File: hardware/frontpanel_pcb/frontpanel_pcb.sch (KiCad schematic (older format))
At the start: 15 parts, among them J1 Conn_02x06_Top_Bottom, Q1 BSS138, U1 291V1, U2 NHD-2.8-25664

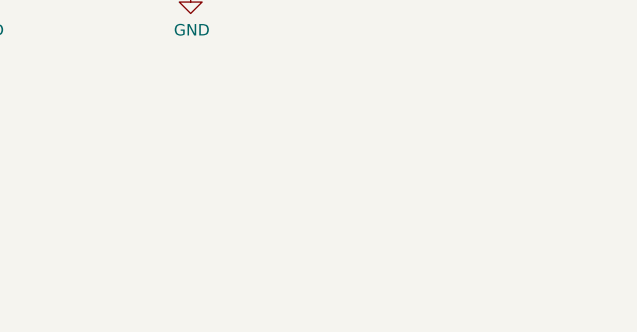
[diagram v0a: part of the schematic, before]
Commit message: hardware: add 2U front / back panel, add Si570 board
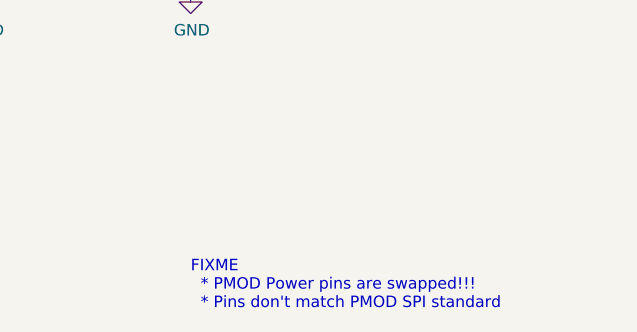
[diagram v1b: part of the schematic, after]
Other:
- note added: "FIXME\n * PMOD Power pins are swapped!!!\n * Pins don't match PMOD SPI standard"
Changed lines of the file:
@@
 Text Label 3600 2250 0    50   ~ 0
 JA8
+Text Notes 7600 6850 0    50   ~ 0
+FIXME\n  * PMOD Power pins are swapped!!!\n  * Pins don't match PMOD SPI standard
 $EndSCHEMATC

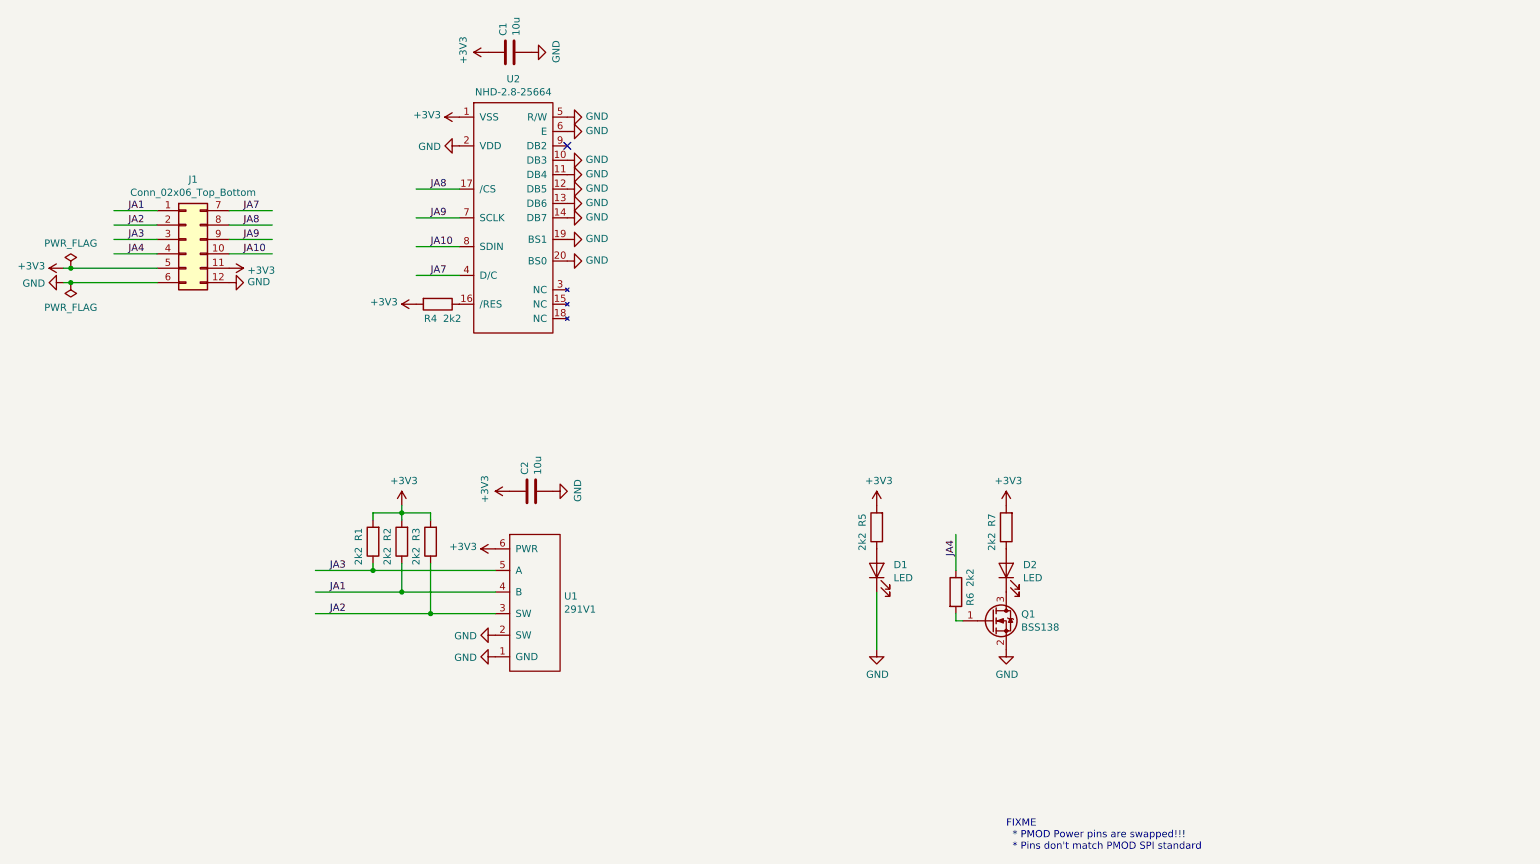
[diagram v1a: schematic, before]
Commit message: Fix display board PMOD pinout
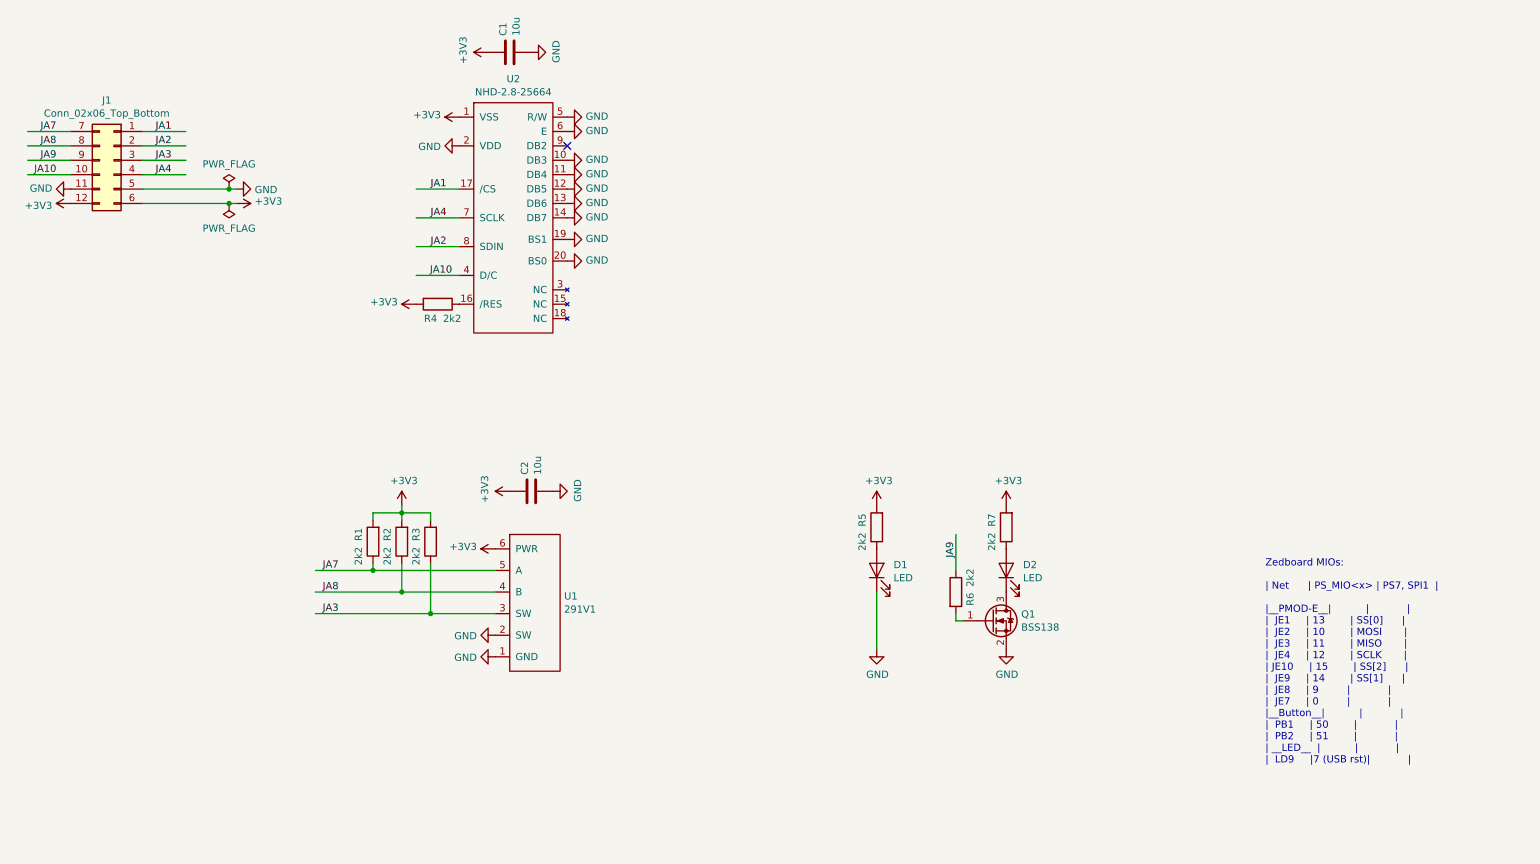
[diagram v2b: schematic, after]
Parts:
- J1: footprint Connector_PinHeader_2.54mm:PinHeader_2x06_P2.54mm_Horizontal -> pmod-conn_6x2:pmod_pin_array_6x2
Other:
- note added: "Zedboard MIOs:\n\n| Net | PS_MIO<x> | PS7, SPI1 |\n\n|__PMOD-E__| | |\n| JE1 | 13 | SS[0] |\n| JE2 | 10 | MOSI |\n| JE3 | 11 | MISO |\n| JE4 | 12 | SCLK |\n| JE10 | 15 | SS[2] |\n| JE9 | 14 | SS[1] |\n| JE8 | 9 | |\n| JE7 | 0 | |\n|__Button__| | |\n| PB1 | 50 | |\n| PB2 | 51 | |\n| __LED__ | | |\n| LD9 |7 (USB rst)| |"
- note removed: "FIXME\n * PMOD Power pins are swapped!!!\n * Pins don't match PMOD SPI standard"
- moved on the sheet: J1
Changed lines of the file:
@@
 	1    0    0    -1
 $EndComp
-Text Label 7250 4800 1    50   ~ 0
-JA4
 $Comp
 L power:+3V3 #PWR0121
@@
 Wire Wire Line
 	2800 4900 3200 4900
-Text Label 2900 5050 0    50   ~ 0
-JA1
-Text Label 2900 5200 0    50   ~ 0
-JA2
 $Comp
 L power:GND #PWR0126
@@
 Wire Wire Line
 	3600 4500 3600 4550
-Text Label 2900 4900 0    50   ~ 0
-JA3
-Text Label 2300 2500 0    50   ~ 0
+Text Label 1000 1950 2    50   ~ 0
 JA8
 Wire Wire Line
-	1700 2500 1400 2500
-Wire Wire Line
-	1700 2700 1400 2700
-Text Label 2300 2400 0    50   ~ 0
+	1600 1950 1900 1950
+Wire Wire Line
+	1600 2150 1900 2150
+Text Label 1000 1850 2    50   ~ 0
 JA7
-Text Label 1500 2400 0    50   ~ 0
+Text Label 1800 1850 2    50   ~ 0
 JA1
-Text Label 1500 2500 0    50   ~ 0
+Text Label 1800 1950 2    50   ~ 0
 JA2
-Text Label 2300 2600 0    50   ~ 0
+Text Label 1000 2050 2    50   ~ 0
 JA9
 $Comp
 L power:GND #PWR0101
 U 1 1 5DB87CBC
-P 2200 2900
-F 0 "#PWR0101" H 2200 2650 50  0001 C CNN
-F 1 "GND" V 2205 2772 50  0000 R CNN
-F 2 "" H 2200 2900 50  0001 C CNN
-F 3 "" H 2200 2900 50  0001 C CNN
-	1    2200 2900
-	0    -1   -1   0
+P 1100 2250
+F 0 "#PWR0101" H 1100 2000 50  0001 C CNN
+F 1 "GND" V 1105 2122 50  0000 R CNN
+F 2 "" H 1100 2250 50  0001 C CNN
+F 3 "" H 1100 2250 50  0001 C CNN
+	1    1100 2250
+	0    1    -1   0
 $EndComp
 $Comp
 L power:GND #PWR0102
 U 1 1 5DB8833E
-P 1050 2900
-F 0 "#PWR0102" H 1050 2650 50  0001 C CNN
-F 1 "GND" V 1055 2772 50  0000 R CNN
-F 2 "" H 1050 2900 50  0001 C CNN
-F 3 "" H 1050 2900 50  0001 C CNN
-	1    1050 2900
-	0    1    1    0
-$EndComp
-Text Label 1500 2700 0    50   ~ 0
+P 2250 2250
+F 0 "#PWR0102" H 2250 2000 50  0001 C CNN
+F 1 "GND" V 2255 2122 50  0000 R CNN
+F 2 "" H 2250 2250 50  0001 C CNN
+F 3 "" H 2250 2250 50  0001 C CNN
+	1    2250 2250
+	0    -1   1    0
+$EndComp
+Text Label 1800 2150 2    50   ~ 0
 JA4
 $Comp
 L Connector_Generic:Conn_02x06_Top_Bottom J1
 U 1 1 5DB867E7
-P 1900 2600
-F 0 "J1" H 1950 3017 50  0000 C CNN
-F 1 "Conn_02x06_Top_Bottom" H 1950 2926 50  0000 C CNN
-F 2 "Connector_PinHeader_2.54mm:PinHeader_2x06_P2.54mm_Horizontal" H 1900 2600 50  0001 C CNN
-F 3 "~" H 1900 2600 50  0001 C CNN
-	1    1900 2600
-	1    0    0    -1
-$EndComp
-Wire Wire Line
-	1700 2600 1400 2600
+P 1400 2050
+F 0 "J1" H 1450 2467 50  0000 C CNN
+F 1 "Conn_02x06_Top_Bottom" H 1450 2376 50  0000 C CNN
+F 2 "pmod-conn_6x2:pmod_pin_array_6x2" H 1400 2050 50  0001 C CNN
+F 3 "~" H 1400 2050 50  0001 C CNN
+	1    1400 2050
+	-1   0    0    -1
+$EndComp
+Wire Wire Line
+	1600 2050 1900 2050
 $Comp
 L power:+3V3 #PWR0104
 U 1 1 5DB8A115
-P 2200 2800
-F 0 "#PWR0104" H 2200 2650 50  0001 C CNN
-F 1 "+3V3" V 2215 2928 50  0000 L CNN
-F 2 "" H 2200 2800 50  0001 C CNN
-F 3 "" H 2200 2800 50  0001 C CNN
-	1    2200 2800
-	0    1    1    0
-$EndComp
-$Comp
-L power:+3V3 #PWR0103
-U 1 1 5DB89814
-P 1050 2800
-F 0 "#PWR0103" H 1050 2650 50  0001 C CNN
-F 1 "+3V3" V 1065 2928 50  0000 L CNN
-F 2 "" H 1050 2800 50  0001 C CNN
-F 3 "" H 1050 2800 50  0001 C CNN
-	1    1050 2800
-	0    -1   -1   0
-$EndComp
-Text Label 1500 2600 0    50   ~ 0
+P 1100 2350
+F 0 "#PWR0104" H 1100 2200 50  0001 C CNN
+F 1 "+3V3" V 1115 2478 50  0000 L CNN
+F 2 "" H 1100 2350 50  0001 C CNN
+F 3 "" H 1100 2350 50  0001 C CNN
+	1    1100 2350
+	0    -1   1    0
+$EndComp
+Text Label 1800 2050 2    50   ~ 0
 JA3
 Wire Wire Line
-	1700 2400 1400 2400
-Wire Wire Line
-	1050 2800 1100 2800
-Wire Wire Line
-	1050 2900 1100 2900
+	1600 1850 1900 1850
+Wire Wire Line
+	2250 2250 2200 2250
+Wire Wire Line
+	2250 2350 2200 2350
 $Comp
 L power:PWR_FLAG #FLG0101
 U 1 1 5DC1EEBC
-P 1100 2800
-F 0 "#FLG0101" H 1100 2875 50  0001 C CNN
-F 1 "PWR_FLAG" H 1100 2973 50  0000 C CNN
-F 2 "" H 1100 2800 50  0001 C CNN
-F 3 "~" H 1100 2800 50  0001 C CNN
-	1    1100 2800
-	1    0    0    -1
+P 2200 2250
+F 0 "#FLG0101" H 2200 2325 50  0001 C CNN
+F 1 "PWR_FLAG" H 2200 2423 50  0000 C CNN
+F 2 "" H 2200 2250 50  0001 C CNN
+F 3 "~" H 2200 2250 50  0001 C CNN
+	1    2200 2250
+	-1   0    0    -1
 $EndComp
 $Comp
 L power:PWR_FLAG #FLG0102
 U 1 1 5DC1F507
-P 1100 2900
-F 0 "#FLG0102" H 1100 2975 50  0001 C CNN
-F 1 "PWR_FLAG" H 1100 3073 50  0000 C CNN
-F 2 "" H 1100 2900 50  0001 C CNN
-F 3 "~" H 1100 2900 50  0001 C CNN
-	1    1100 2900
-	-1   0    0    1
-$EndComp
-Connection ~ 1100 2800
-Wire Wire Line
-	1100 2800 1700 2800
-Connection ~ 1100 2900
-Wire Wire Line
-	1100 2900 1700 2900
+P 2200 2350
+F 0 "#FLG0102" H 2200 2425 50  0001 C CNN
+F 1 "PWR_FLAG" H 2200 2523 50  0000 C CNN
+F 2 "" H 2200 2350 50  0001 C CNN
+F 3 "~" H 2200 2350 50  0001 C CNN
+	1    2200 2350
+	1    0    0    1
+$EndComp
+Connection ~ 2200 2250
+Wire Wire Line
+	2200 2250 1600 2250
+Connection ~ 2200 2350
+Wire Wire Line
+	2200 2350 1600 2350
 $Comp
 L Device:C C2
@@
 	0    -1   -1   0
 $EndComp
-Text Label 2300 2700 0    50   ~ 0
+Text Label 1000 2150 2    50   ~ 0
 JA10
 Wire Wire Line
-	2200 2400 2500 2400
-Wire Wire Line
-	2200 2500 2500 2500
-Wire Wire Line
-	2200 2600 2500 2600
-Wire Wire Line
-	2200 2700 2500 2700
+	1100 1850 800  1850
+Wire Wire Line
+	1100 1950 800  1950
+Wire Wire Line
+	1100 2050 800  2050
+Wire Wire Line
+	1100 2150 800  2150
 Wire Wire Line
 	3500 2450 3800 2450
 Wire Wire Line
 	3500 2650 3800 2650
-Text Label 3600 2850 0    50   ~ 0
+$Comp
+L power:+3V3 #PWR0103
+U 1 1 5DB89814
+P 2250 2350
+F 0 "#PWR0103" H 2250 2200 50  0001 C CNN
+F 1 "+3V3" V 2265 2478 50  0000 L CNN
+F 2 "" H 2250 2350 50  0001 C CNN
+F 3 "" H 2250 2350 50  0001 C CNN
+	1    2250 2350
+	0    1    -1   0
+$EndComp
+Text Label 3600 2250 0    50   ~ 0
+JA1
+Text Label 3600 2650 0    50   ~ 0
+JA2
+Text Label 2850 5200 0    50   ~ 0
+JA3
+Text Label 3600 2450 0    50   ~ 0
+JA4
+Text Label 3750 2850 2    50   ~ 0
+JA10
+Text Label 7250 4700 3    50   ~ 0
+JA9
+Text Label 2850 5050 0    50   ~ 0
+JA8
+Text Label 2850 4900 0    50   ~ 0
 JA7
-Text Label 3600 2450 0    50   ~ 0
-JA9
-Text Label 3600 2650 0    50   ~ 0
-JA10
-Text Label 3600 2250 0    50   ~ 0
-JA8
-Text Notes 7600 6850 0    50   ~ 0
-FIXME\n  * PMOD Power pins are swapped!!!\n  * Pins don't match PMOD SPI standard
+Text Notes 9400 6250 0    50   ~ 0
+Zedboard MIOs:\n\n| Net      | PS_MIO<x> | PS7, SPI1  |\n\n|__PMOD-E__|           |            |\n|  JE1     | 13        | SS[0]      |\n|  JE2     | 10        | MOSI       |\n|  JE3     | 11        | MISO       |\n|  JE4     | 12        | SCLK       |\n| JE10     | 15        | SS[2]      |\n|  JE9     | 14        | SS[1]      |\n|  JE8     | 9         |            |\n|  JE7     | 0         |            |\n|__Button__|           |            |\n|  PB1     | 50        |            |\n|  PB2     | 51        |            |\n| __LED__  |           |            |\n|  LD9     |7 (USB rst)|            |
 $EndSCHEMATC
